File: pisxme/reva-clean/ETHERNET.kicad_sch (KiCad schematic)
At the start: 4 parts, among them J2 A70-112-331N126, U6 TPD4E004DRYR, U9 TPD4E004DRYR, X6 ETHERNET_Contract

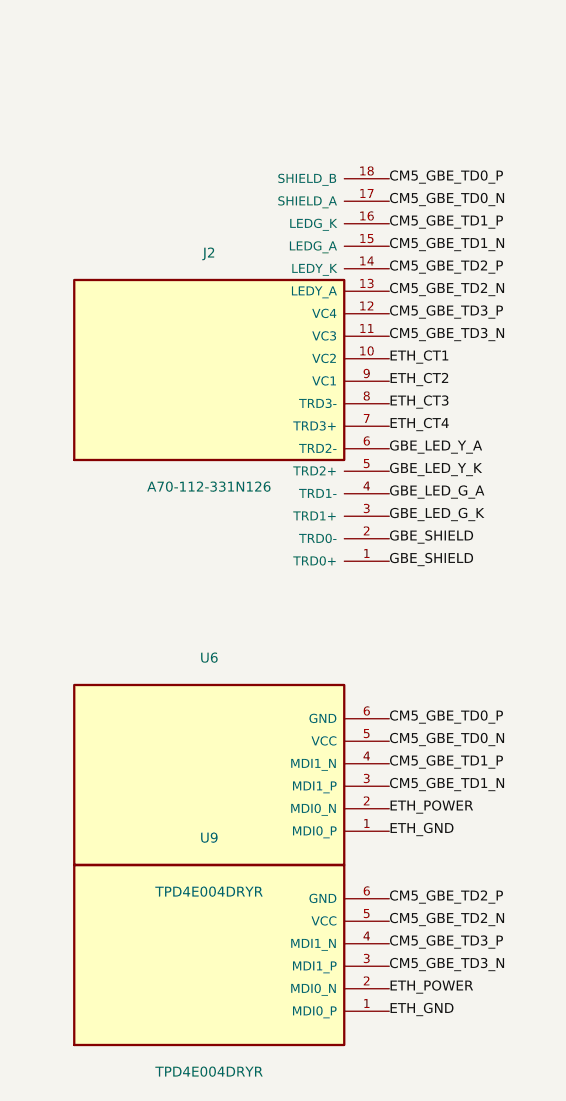
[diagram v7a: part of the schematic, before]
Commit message: phase17: repair Ethernet net authority
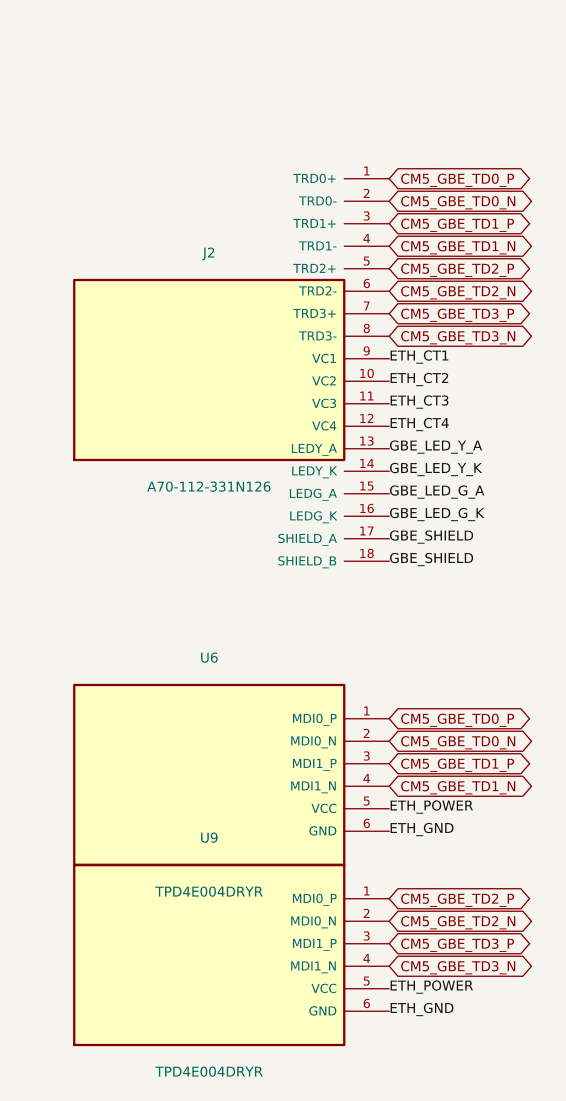
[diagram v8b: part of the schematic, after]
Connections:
- net CM5_GBE_TD0_N: now also J2.2 (TRD0-), U6.2 (MDI0_N); no longer J2.17 (SHIELD_A), U6.5 (VCC)
- net CM5_GBE_TD0_P: now also J2.1 (TRD0+), U6.1 (MDI0_P); no longer J2.18 (SHIELD_B), U6.6 (GND)
- net CM5_GBE_TD1_N: now also J2.4 (TRD1-), U6.4 (MDI1_N); no longer J2.15 (LEDG_A), U6.3 (MDI1_P)
- net CM5_GBE_TD1_P: now also J2.3 (TRD1+), U6.3 (MDI1_P); no longer J2.16 (LEDG_K), U6.4 (MDI1_N)
- net CM5_GBE_TD2_N: now also J2.6 (TRD2-), U9.2 (MDI0_N); no longer J2.13 (LEDY_A), U9.5 (VCC)
- net CM5_GBE_TD2_P: now also J2.5 (TRD2+), U9.1 (MDI0_P); no longer J2.14 (LEDY_K), U9.6 (GND)
- net CM5_GBE_TD3_N: now also J2.8 (TRD3-), U9.4 (MDI1_N); no longer J2.11 (VC3), U9.3 (MDI1_P)
- net CM5_GBE_TD3_P: now also J2.7 (TRD3+), U9.3 (MDI1_P); no longer J2.12 (VC4), U9.4 (MDI1_N)
- net ETH_CT1: now also J2.9 (VC1); no longer J2.10 (VC2)
- net ETH_CT2: now also J2.10 (VC2); no longer J2.9 (VC1)
- net ETH_CT3: now also J2.11 (VC3); no longer J2.8 (TRD3-)
- net ETH_CT4: now also J2.12 (VC4); no longer J2.7 (TRD3+)
- net ETH_GND: now also U6.6 (GND), U9.6 (GND); no longer U6.1 (MDI0_P), U9.1 (MDI0_P)
- net ETH_POWER: now also U6.5 (VCC), U9.5 (VCC); no longer U6.2 (MDI0_N), U9.2 (MDI0_N)
- net GBE_LED_G_A: now also J2.15 (LEDG_A); no longer J2.4 (TRD1-)
- net GBE_LED_G_K: now also J2.16 (LEDG_K); no longer J2.3 (TRD1+)
- net GBE_LED_Y_A: now also J2.13 (LEDY_A); no longer J2.6 (TRD2-)
- net GBE_LED_Y_K: now also J2.14 (LEDY_K); no longer J2.5 (TRD2+)
- net GBE_SHIELD: now also J2.17 (SHIELD_A), J2.18 (SHIELD_B); no longer J2.1 (TRD0+), J2.2 (TRD0-)
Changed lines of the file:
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@@
       (path "/30000000-0000-0000-0000-000000000000/10000000-0000-0000-0000-000000000006" (reference "X6" ) (unit 1))))
   )
-(label "CM5_GBE_TD0_P" (at 70 78.75 0) (effects (font (size 1.1 1.1)) (justify left)))
-(label "CM5_GBE_TD0_N" (at 70 81.25 0) (effects (font (size 1.1 1.1)) (justify left)))
-(label "CM5_GBE_TD1_P" (at 70 83.75 0) (effects (font (size 1.1 1.1)) (justify left)))
-(label "CM5_GBE_TD1_N" (at 70 86.25 0) (effects (font (size 1.1 1.1)) (justify left)))
-(label "CM5_GBE_TD2_P" (at 70 88.75 0) (effects (font (size 1.1 1.1)) (justify left)))
-(label "CM5_GBE_TD2_N" (at 70 91.25 0) (effects (font (size 1.1 1.1)) (justify left)))
-(label "CM5_GBE_TD3_P" (at 70 93.75 0) (effects (font (size 1.1 1.1)) (justify left)))
-(label "CM5_GBE_TD3_N" (at 70 96.25 0) (effects (font (size 1.1 1.1)) (justify left)))
+(global_label "CM5_GBE_TD0_P" (shape bidirectional) (at 70 78.75 0) (effects (font (size 1.1 1.1)) (justify left)))
+(global_label "CM5_GBE_TD0_N" (shape bidirectional) (at 70 81.25 0) (effects (font (size 1.1 1.1)) (justify left)))
+(global_label "CM5_GBE_TD1_P" (shape bidirectional) (at 70 83.75 0) (effects (font (size 1.1 1.1)) (justify left)))
+(global_label "CM5_GBE_TD1_N" (shape bidirectional) (at 70 86.25 0) (effects (font (size 1.1 1.1)) (justify left)))
+(global_label "CM5_GBE_TD2_P" (shape bidirectional) (at 70 88.75 0) (effects (font (size 1.1 1.1)) (justify left)))
+(global_label "CM5_GBE_TD2_N" (shape bidirectional) (at 70 91.25 0) (effects (font (size 1.1 1.1)) (justify left)))
+(global_label "CM5_GBE_TD3_P" (shape bidirectional) (at 70 93.75 0) (effects (font (size 1.1 1.1)) (justify left)))
+(global_label "CM5_GBE_TD3_N" (shape bidirectional) (at 70 96.25 0) (effects (font (size 1.1 1.1)) (justify left)))
 (label "ETH_CT1" (at 70 98.75 0) (effects (font (size 1.1 1.1)) (justify left)))
 (label "ETH_CT2" (at 70 101.25 0) (effects (font (size 1.1 1.1)) (justify left)))
@@
 (pin "17")
 (pin "18") (instances (project "PiSXMe_RevA_Clean" (path "/30000000-0000-0000-0000-000000000000" (reference "J2") (unit 1)))) )
-(label "CM5_GBE_TD0_P" (at 70 138.75 0) (effects (font (size 1.1 1.1)) (justify left)))
-(label "CM5_GBE_TD0_N" (at 70 141.25 0) (effects (font (size 1.1 1.1)) (justify left)))
-(label "CM5_GBE_TD1_P" (at 70 143.75 0) (effects (font (size 1.1 1.1)) (justify left)))
-(label "CM5_GBE_TD1_N" (at 70 146.25 0) (effects (font (size 1.1 1.1)) (justify left)))
+(global_label "CM5_GBE_TD0_P" (shape bidirectional) (at 70 138.75 0) (effects (font (size 1.1 1.1)) (justify left)))
+(global_label "CM5_GBE_TD0_N" (shape bidirectional) (at 70 141.25 0) (effects (font (size 1.1 1.1)) (justify left)))
+(global_label "CM5_GBE_TD1_P" (shape bidirectional) (at 70 143.75 0) (effects (font (size 1.1 1.1)) (justify left)))
+(global_label "CM5_GBE_TD1_N" (shape bidirectional) (at 70 146.25 0) (effects (font (size 1.1 1.1)) (justify left)))
 (label "ETH_POWER" (at 70 148.75 0) (effects (font (size 1.1 1.1)) (justify left)))
 (label "ETH_GND" (at 70 151.25 0) (effects (font (size 1.1 1.1)) (justify left)))
@@
 (pin "4")
 (pin "5")
-(pin "6") (instances (project "PiSXMe_RevA_Clean" (path "/30000000-0000-0000-0000-000000000000" (reference "U6") (unit 1)))) )(label "CM5_GBE_TD2_P" (at 70 158.75 0) (effects (font (size 1.1 1.1)) (justify left)))
-(label "CM5_GBE_TD2_N" (at 70 161.25 0) (effects (font (size 1.1 1.1)) (justify left)))
-(label "CM5_GBE_TD3_P" (at 70 163.75 0) (effects (font (size 1.1 1.1)) (justify left)))
-(label "CM5_GBE_TD3_N" (at 70 166.25 0) (effects (font (size 1.1 1.1)) (justify left)))
+(pin "6") (instances (project "PiSXMe_RevA_Clean" (path "/30000000-0000-0000-0000-000000000000" (reference "U6") (unit 1)))) )(global_label "CM5_GBE_TD2_P" (shape bidirectional) (at 70 158.75 0) (effects (font (size 1.1 1.1)) (justify left)))
+(global_label "CM5_GBE_TD2_N" (shape bidirectional) (at 70 161.25 0) (effects (font (size 1.1 1.1)) (justify left)))
+(global_label "CM5_GBE_TD3_P" (shape bidirectional) (at 70 163.75 0) (effects (font (size 1.1 1.1)) (justify left)))
+(global_label "CM5_GBE_TD3_N" (shape bidirectional) (at 70 166.25 0) (effects (font (size 1.1 1.1)) (justify left)))
 (label "ETH_POWER" (at 70 168.75 0) (effects (font (size 1.1 1.1)) (justify left)))
 (label "ETH_GND" (at 70 171.25 0) (effects (font (size 1.1 1.1)) (justify left)))
